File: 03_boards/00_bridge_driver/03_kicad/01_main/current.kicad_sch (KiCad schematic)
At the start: 22 parts, among them U10 INA241A3xD, U11 INA241A3xD, U12 AMC1311, U13 AMC1311

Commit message: Draft Schematic Finished
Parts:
- added R37, R39: 10k, symbol Device:R
- added R38, R40: 15k, symbol Device:R
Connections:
- net +12VIS: now also U10.7 (REF1), U11.7 (REF1)
- net +3.3VIS: no longer U10.7 (REF1), U11.7 (REF1)
- net I_CS1_OUT: now also R37.2, R38.1, R39.2, R40.1; no longer U11.5, U13.2 (VINP)
- net I_CS2_OUT: now also U13.2 (VINP); no longer U10.5
- net PGND: now also R38.2, R40.2
- new net: R37.1, U11.5
- new net: R39.1, U10.5
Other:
- moved on the sheet: U10, U11

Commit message: Simulation for current sensors and such
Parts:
- removed R37, R39: 10k, symbol Device:R
- removed R38, R40: 15k, symbol Device:R
- removed U10, U11: INA241A3xD, Package_SO:SOIC-8_3.9x4.9mm_P1.27mm, symbol Amplifier_Current:INA241A3xD
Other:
- note added: "F, C"
- title: (none) -> Current Sensors & Isolation

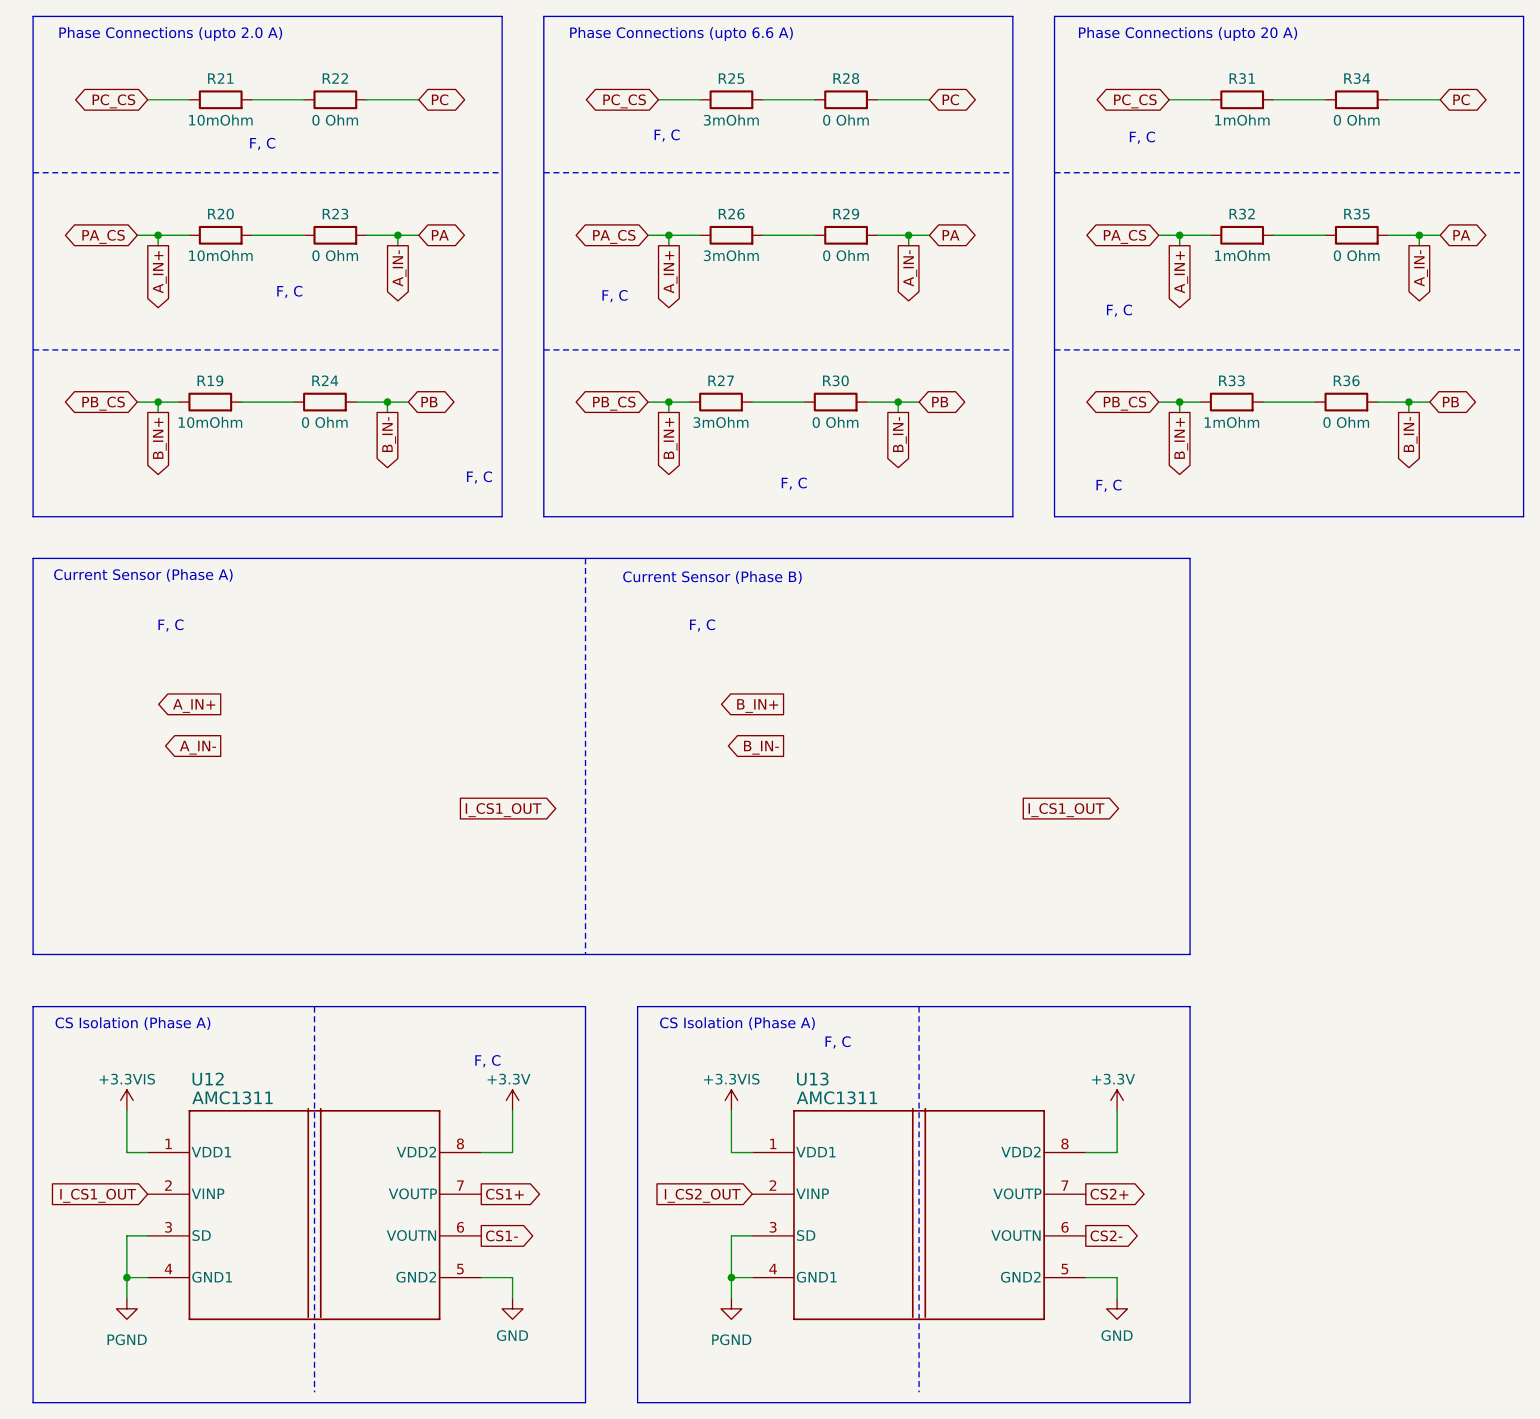
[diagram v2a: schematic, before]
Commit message: Week 0x9 | Nearly there! (#38)
* Updated readmes formatting & other files

* Removed no commercial aspiration notes and added a simple status section for the readme

* Made the status section inline

* Forgot a full stop.

* Added application notes to docs/readme.md

* Added current state and terminal state on the application notes series

* Added .md instead of .csv for BOM

* Added BOM for bridge driver and updated the - to em

* Added 04_procurement folders and made 04_media into 05_media

* Added fixture folder and moved docs to 00

* Technically I have done that just by the bridge driver design.

* Added checking system for BOM and added 05_media section for bridge driver

* Added the order for magnetic encoder

* Added the the link to the digikey file.

* Updated media & readmes to reflect that

* Got the digikey BOM and also checked the list off for armature board

* Nearly finished the schematic for driver board

* Added a some code and fixed the derived.ut vs metric.ut referencing mistake

* Finished Driver Board Schematic.

* More footprint selection. YAY

* More footprints.

* Footprints finished and hence initial BOM based on footprints is also

* Updated schematic.

* Improving the unit boundary and notes for 00_analytical

* Updated main readme to reflect work done this week.

* Removed the line about the integrated sensor board. it's literally below it.

* Rewrote fabrication note.

* Update README.md

* Updated readmes and added the bowley system logo

* Made it clear the values and updated the schematics.

* Updated comment to design not development. they mean different things.

* deleted .csv -> Who uses it anyways!?

* Initial PCB modelling work

* Added work so far on bridge driver. Took some pics and updates readmes.

* Updated to doubles images (back and front)
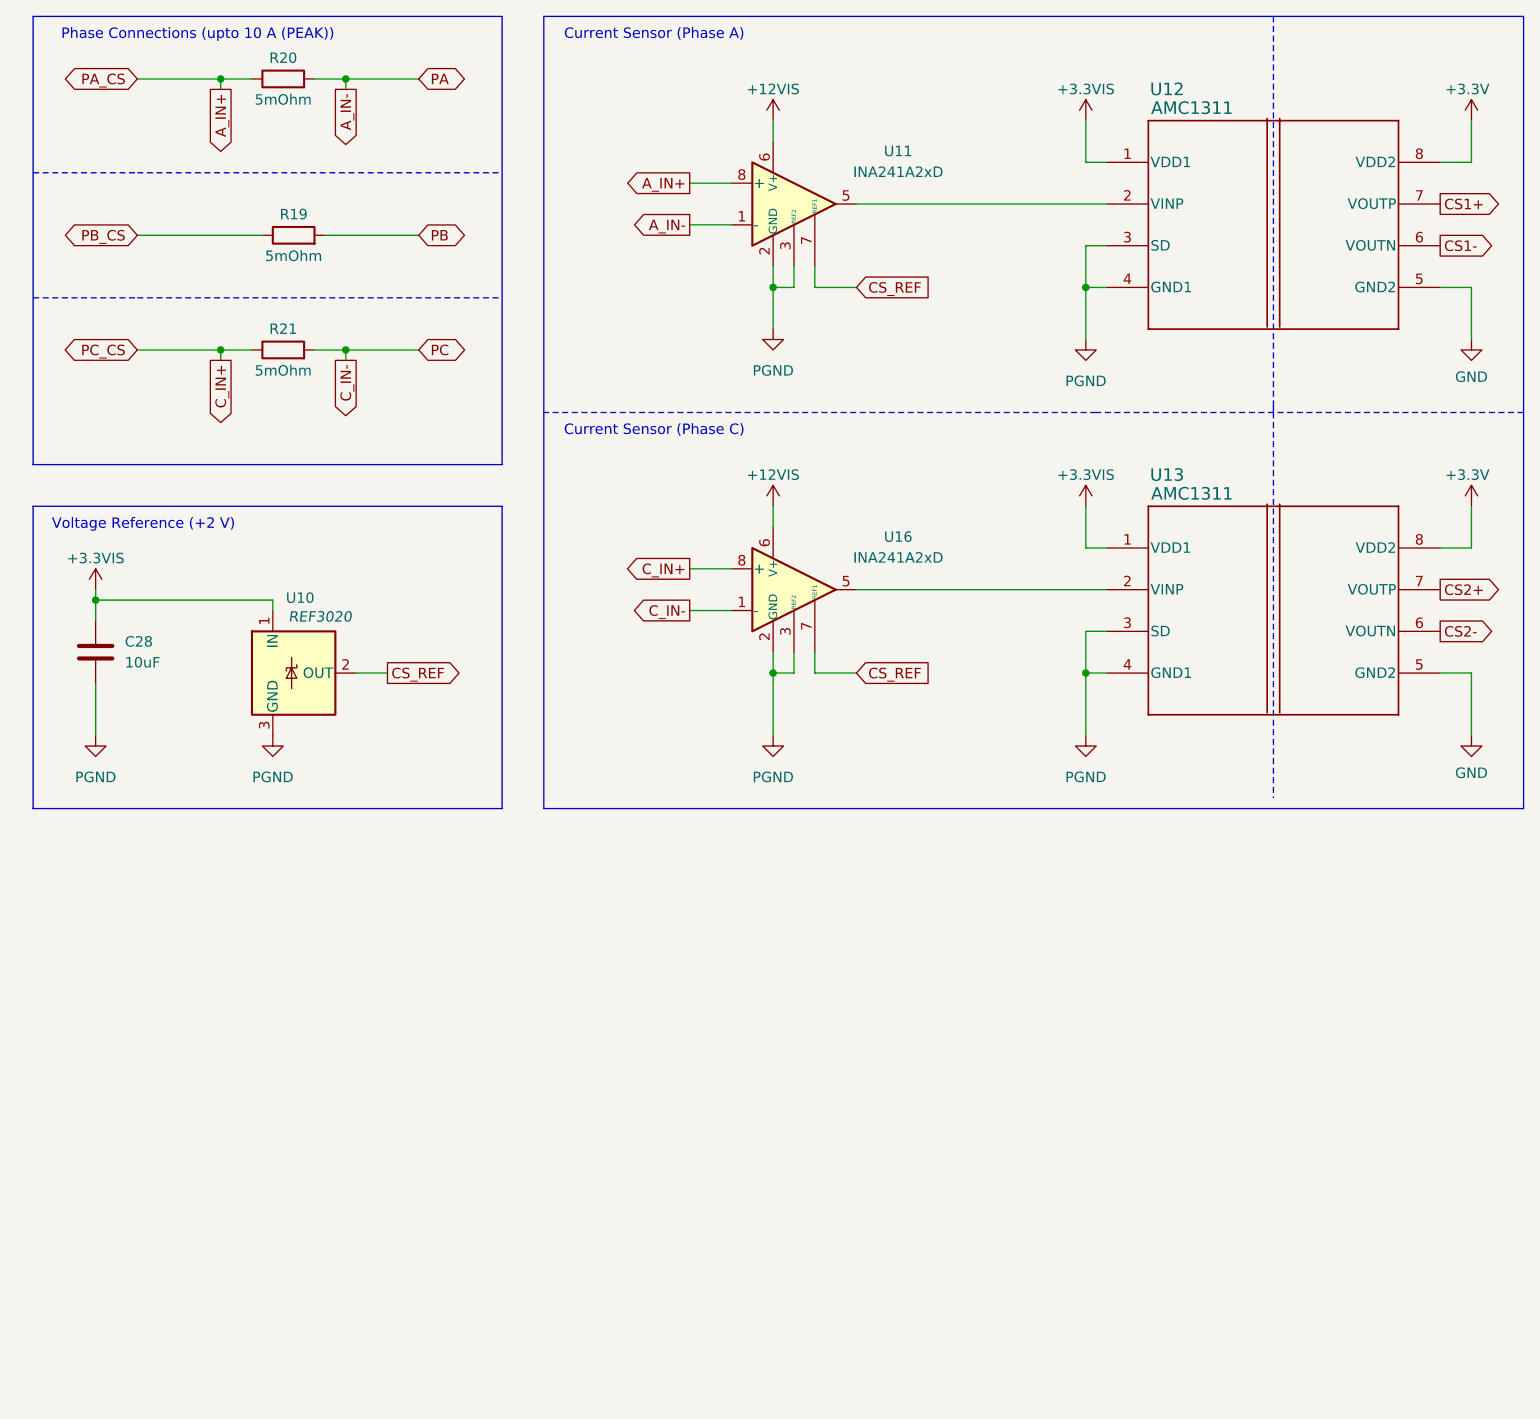
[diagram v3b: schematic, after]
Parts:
- removed R22, R23, R24, R28, R29, R30, R34, R35, R36: 0 Ohm, symbol Device:R
- removed R25, R26, R27: 3mOhm, symbol Device:R
- removed R31, R32, R33: 1mOhm, symbol Device:R
- added C28: 10uF, Capacitor_SMD:C_1206_3216Metric, symbol Device:C
- added U10: REF3020, Package_TO_SOT_SMD:SOT-23, symbol Reference_Voltage:REF3020
- added U11, U16: INA241A2xD, Package_SO:SOIC-8_3.9x4.9mm_P1.27mm, symbol Amplifier_Current:INA241A2xD
- R19, R20, R21: value 10mOhm -> 5mOhm; footprint (none) -> Resistor_SMD:R_2512_6332Metric
- U12, U13: footprint DWV0008A -> AMC1311DWVR:DWV0008A
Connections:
- net +3.3VIS: now also C28.1, U10.1 (IN)
- net A_IN+: now also U11.8 (+)
- net A_IN-: now also R20.2, U11.1 (-)
- net PGND: now also C28.2, U10.3 (GND), U11.2 (GND), U11.3 (REF2), U11.4 (GND), U16.2 (GND), U16.3 (REF2), U16.4 (GND)
- net PB: now reaches R19.2
- net C_IN-: now reaches R21.2
- net C_IN-: now also U16.1 (-)
- net B_IN+ renamed PB_CS
- net I_CS1_OUT: no longer names the net of U12.2 (VINP)
- net I_CS1_OUT: now also U11.5
- net I_CS2_OUT: no longer names the net of U13.2 (VINP)
- net I_CS2_OUT: now also U16.5
- net PC_CS renamed C_IN+
- net C_IN+: now also U16.8 (+)
- new net +12VIS: U11.6 (V+), U16.6 (V+)
- new net CS_REF: U10.2 (OUT), U11.7 (REF1), U16.7 (REF1)
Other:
- note added: "Current Sensor (Phase C)"
- note added: "Phase Connections (upto 10 A (PEAK))"
- note added: "Voltage Reference (+2 V)"
- note removed: "CS Isolation (Phase A)"
- note removed: "Current Sensor (Phase B)"
- note removed: "F, C"
- note removed: "Phase Connections (upto 2.0 A)"
- note removed: "Phase Connections (upto 20 A)"
- note removed: "Phase Connections (upto 6.6 A)"
- moved on the sheet: R19, R20, R21, U12, U13
